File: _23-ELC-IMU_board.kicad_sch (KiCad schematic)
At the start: 4 parts

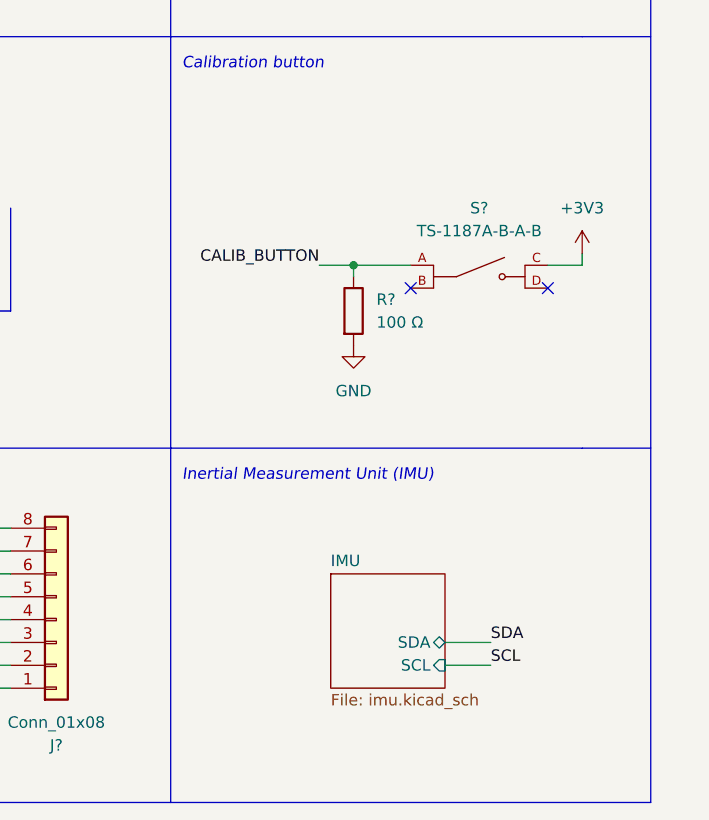
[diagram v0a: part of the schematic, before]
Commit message: Added test points for I2C
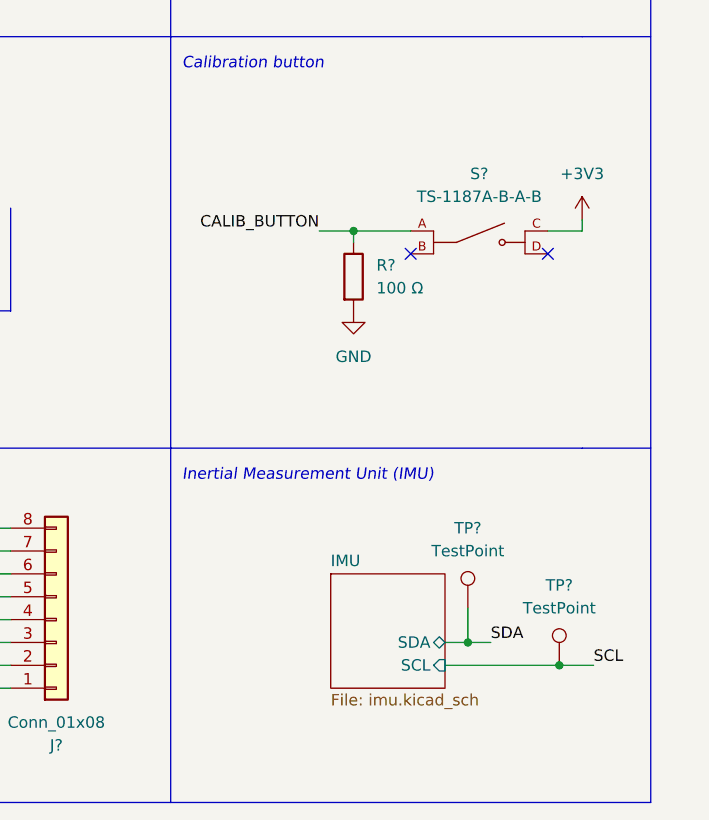
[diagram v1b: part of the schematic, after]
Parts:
- added TP? (x2): TestPoint, symbol Connector:TestPoint
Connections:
- net SCL: now also TP?.1
- net SDA: now also TP?.1
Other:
- moved on the sheet: R?, S?

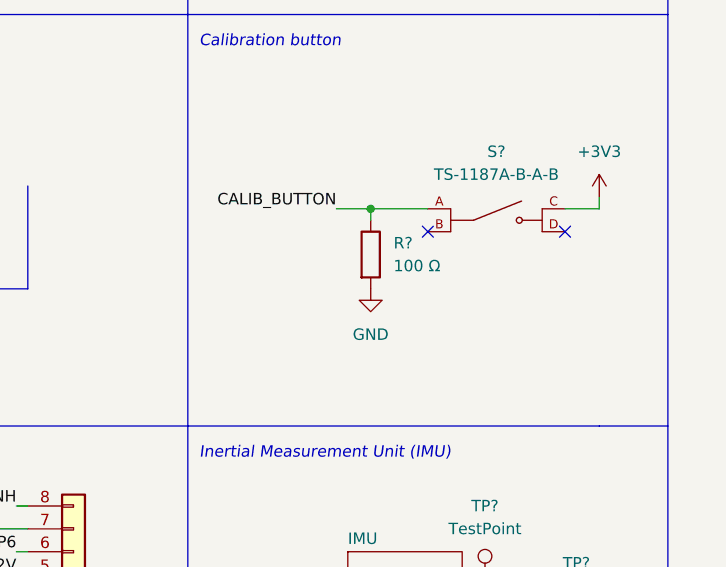
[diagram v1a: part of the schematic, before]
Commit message: 100 ohm => 1 kOhm
Pull down probably too low
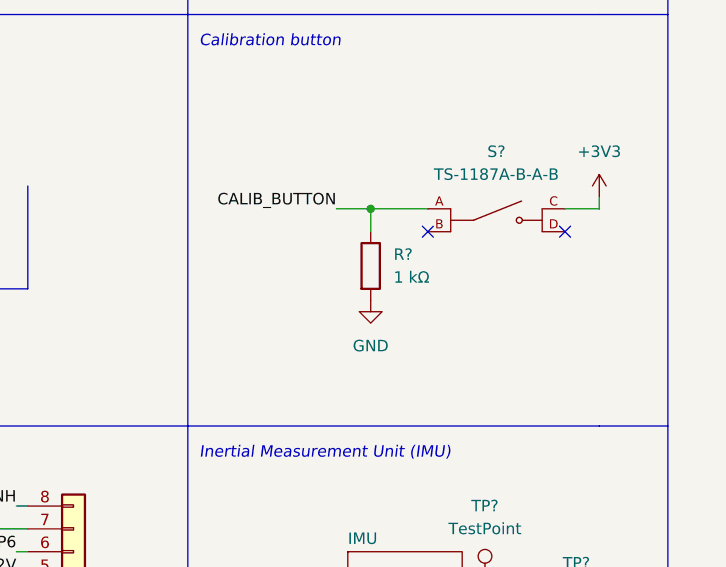
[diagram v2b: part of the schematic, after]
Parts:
- R?: value 100 Ω -> 1 kΩ
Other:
- moved on the sheet: R?
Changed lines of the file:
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@@
     (stroke (width 0) (type default) (color 0 0 0 0))
   )
-  (wire (pts (xy 180.34 95.25) (xy 180.34 96.52))
+  (wire (pts (xy 180.34 95.25) (xy 180.34 97.79))
     (stroke (width 0) (type default) (color 0 0 0 0))
   )
@@
     (pin "1")
   )
-  (symbol (lib_id "Device:R") (at 180.34 100.33 0) (unit 1)
-    (in_bom yes) (on_board yes) (fields_autoplaced)
-    (property "Reference" "R?" (id 0) (at 182.88 99.0599 0)
-      (effects (font (size 1.27 1.27)) (justify left))
-    )
-    (property "Value" "100 Ω" (id 1) (at 182.88 101.5999 0)
-      (effects (font (size 1.27 1.27)) (justify left))
-    )
-    (property "Footprint" "Resistor_SMD:R_0201_0603Metric" (id 2) (at 178.562 100.33 90)
-      (effects (font (size 1.27 1.27)) hide)
-    )
-    (property "Datasheet" "~" (id 3) (at 180.34 100.33 0)
+  (symbol (lib_id "Device:R") (at 180.34 101.6 0) (unit 1)
+    (in_bom yes) (on_board yes) (fields_autoplaced)
+    (property "Reference" "R?" (id 0) (at 182.88 100.3299 0)
+      (effects (font (size 1.27 1.27)) (justify left))
+    )
+    (property "Value" "1 kΩ" (id 1) (at 182.88 102.8699 0)
+      (effects (font (size 1.27 1.27)) (justify left))
+    )
+    (property "Footprint" "Resistor_SMD:R_0201_0603Metric" (id 2) (at 178.562 101.6 90)
+      (effects (font (size 1.27 1.27)) hide)
+    )
+    (property "Datasheet" "~" (id 3) (at 180.34 101.6 0)
       (effects (font (size 1.27 1.27)) hide)
     )
@@
     (pin "1")
   )
-  (symbol (lib_id "power:GND") (at 180.34 104.14 0) (unit 1)
-    (in_bom yes) (on_board yes) (fields_autoplaced)
-    (property "Reference" "#PWR?" (id 0) (at 180.34 110.49 0)
-      (effects (font (size 1.27 1.27)) hide)
-    )
-    (property "Value" "GND" (id 1) (at 180.34 109.22 0))
-    (property "Footprint" "" (id 2) (at 180.34 104.14 0)
-      (effects (font (size 1.27 1.27)) hide)
-    )
-    (property "Datasheet" "" (id 3) (at 180.34 104.14 0)
+  (symbol (lib_id "power:GND") (at 180.34 105.41 0) (unit 1)
+    (in_bom yes) (on_board yes) (fields_autoplaced)
+    (property "Reference" "#PWR?" (id 0) (at 180.34 111.76 0)
+      (effects (font (size 1.27 1.27)) hide)
+    )
+    (property "Value" "GND" (id 1) (at 180.34 110.49 0))
+    (property "Footprint" "" (id 2) (at 180.34 105.41 0)
+      (effects (font (size 1.27 1.27)) hide)
+    )
+    (property "Datasheet" "" (id 3) (at 180.34 105.41 0)
       (effects (font (size 1.27 1.27)) hide)
     )
@@
     )
     (path "/a06d3903-222c-4eb8-bb14-5ed150152b48"
-      (reference "R?") (unit 1) (value "100 Ω") (footprint "Resistor_SMD:R_0201_0603Metric")
+      (reference "R?") (unit 1) (value "1 kΩ") (footprint "Resistor_SMD:R_0201_0603Metric")
     )
     (path "/20fcfeb0-ed28-45b7-bc17-0a1a87e552cb/d2fa6f23-28b3-495b-8856-8c8bf7f687e9"

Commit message: Updated subsheets
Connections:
- net DIRTY_12V renamed +24V
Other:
- removed sheet Standardized VRMS
- added sheet VRMS (vrmsv2.kicad_sch)
- moved on the sheet: TP?

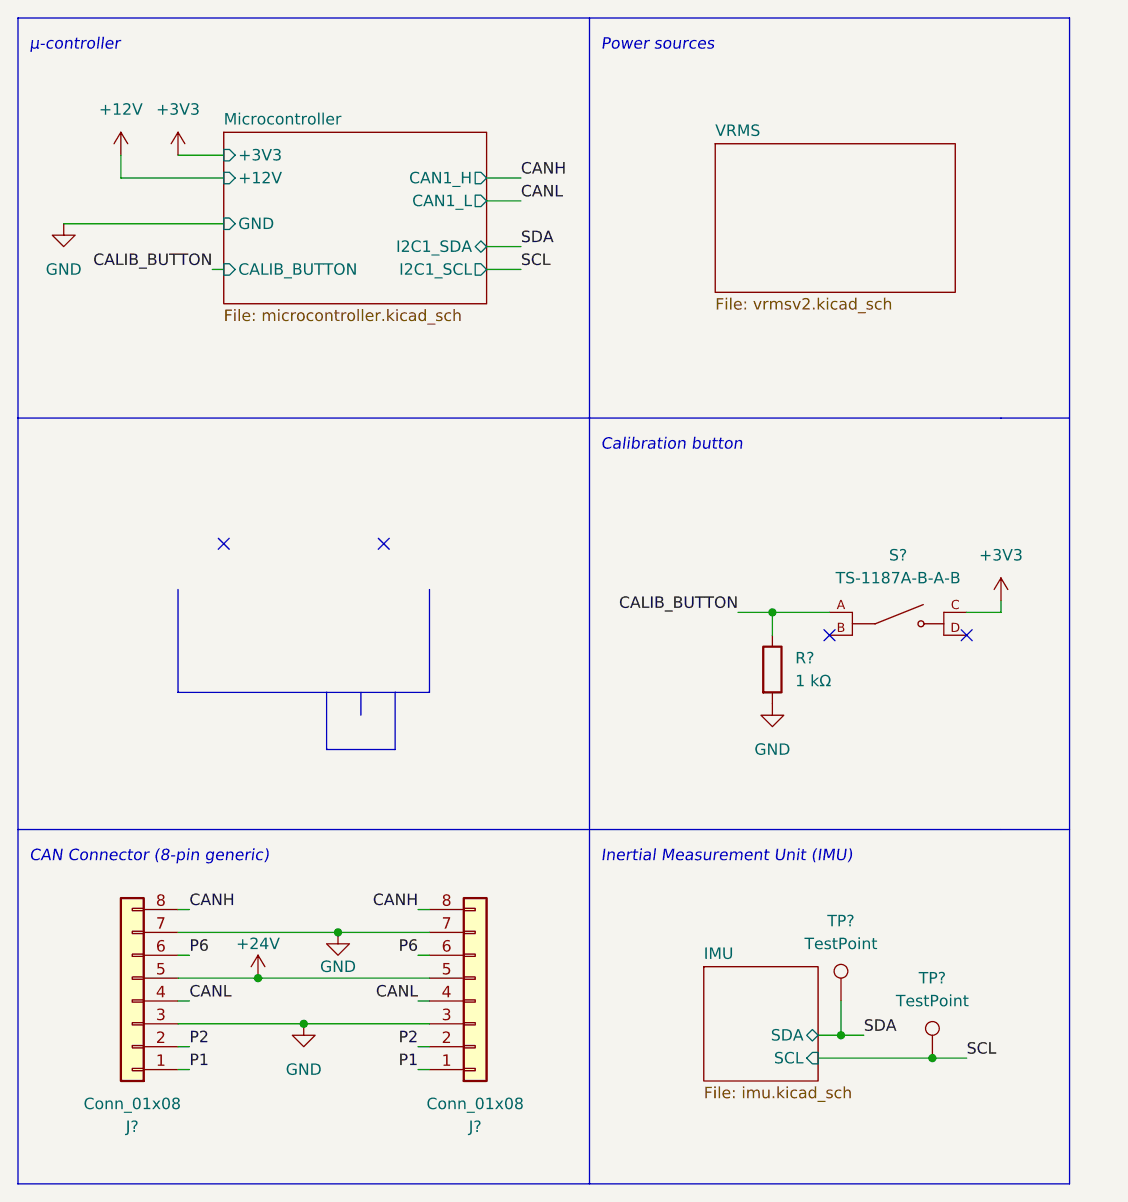
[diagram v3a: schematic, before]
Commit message: Adjusted CAN bus voltage to 5V
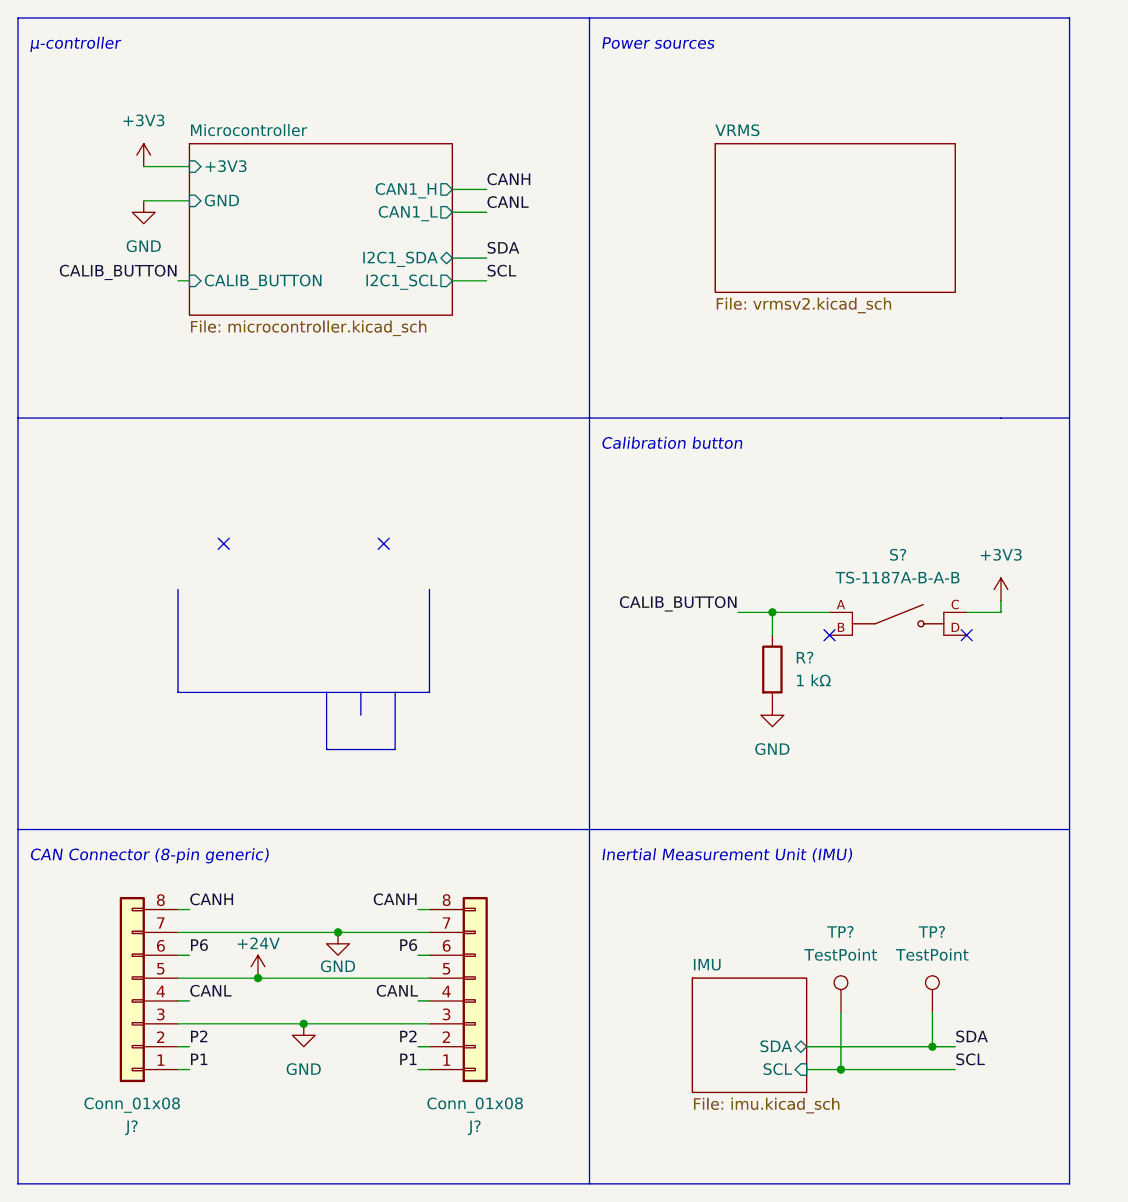
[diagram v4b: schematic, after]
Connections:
- net SCL: now also TP?.1; no longer TP?.1
- net SDA: now also TP?.1; no longer TP?.1
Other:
- sheet Microcontroller ports: added none; removed +12V
- moved on the sheet: TP?

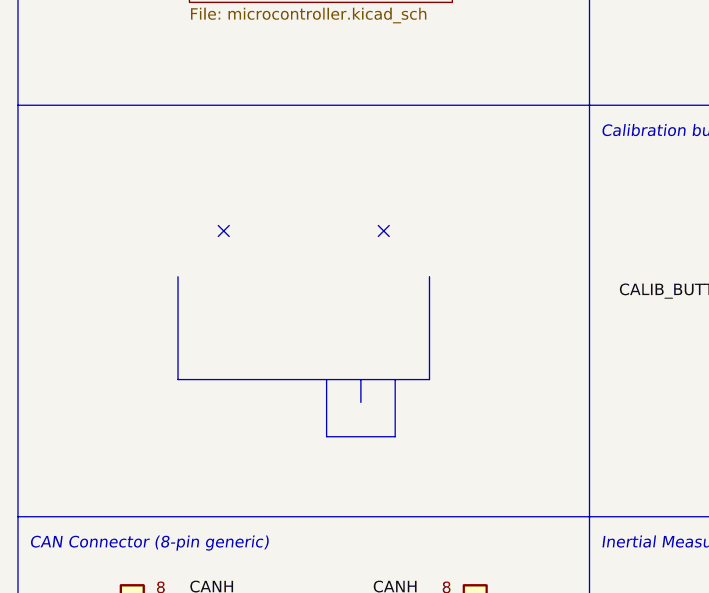
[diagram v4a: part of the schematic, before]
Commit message: Added three mounting holes
I have no idea what to do here
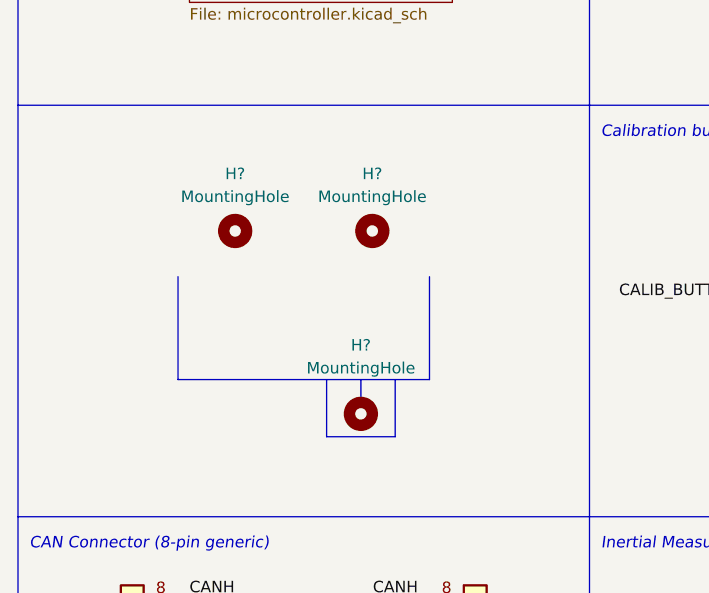
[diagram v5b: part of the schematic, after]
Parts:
- added H? (x3): MountingHole, symbol Mechanical:MountingHole
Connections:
- no-connect marks 4 -> 2
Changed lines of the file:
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@@
   (junction (at 198.12 143.51) (diameter 0) (color 0 0 0 0)
   )
-  (no_connect (at 119.38 87.63))
-  (no_connect (at 137.16 87.63))
   (no_connect (at 201.93 97.79))
   (no_connect (at 186.69 97.79))
@@
     (pin "1")
   )
+  (symbol (lib_id "Mechanical:MountingHole") (at 120.65 87.63 0) (unit 1)
+    (in_bom yes) (on_board yes)
+    (property "Reference" "H?" (id 0) (at 120.65 81.28 0))
+    (property "Value" "MountingHole" (id 1) (at 120.65 83.82 0))
+    (property "Footprint" "" (id 2) (at 120.65 87.63 0)
+      (effects (font (size 1.27 1.27)) hide)
+    )
+    (property "Datasheet" "~" (id 3) (at 120.65 87.63 0)
+      (effects (font (size 1.27 1.27)) hide)
+    )
+  )
+  (symbol (lib_id "Mechanical:MountingHole") (at 135.89 87.63 0) (unit 1)
+    (in_bom yes) (on_board yes)
+    (property "Reference" "H?" (id 0) (at 135.89 81.28 0))
+    (property "Value" "MountingHole" (id 1) (at 135.89 83.82 0))
+    (property "Footprint" "" (id 2) (at 135.89 87.63 0)
+      (effects (font (size 1.27 1.27)) hide)
+    )
+    (property "Datasheet" "~" (id 3) (at 135.89 87.63 0)
+      (effects (font (size 1.27 1.27)) hide)
+    )
+  )
   (symbol (lib_id "power:+3V3") (at 110.49 45.72 0) (unit 1)
     (in_bom yes) (on_board yes) (fields_autoplaced)
@@
     )
     (pin "1")
+  )
+  (symbol (lib_id "Mechanical:MountingHole") (at 134.62 107.95 0) (unit 1)
+    (in_bom yes) (on_board yes)
+    (property "Reference" "H?" (id 0) (at 134.62 100.33 0))
+    (property "Value" "MountingHole" (id 1) (at 134.62 102.87 0))
+    (property "Footprint" "" (id 2) (at 134.62 107.95 0)
+      (effects (font (size 1.27 1.27)) hide)
+    )
+    (property "Datasheet" "~" (id 3) (at 134.62 107.95 0)
+      (effects (font (size 1.27 1.27)) hide)
+    )
   )
   (symbol (lib_id "Device:R") (at 180.34 101.6 0) (unit 1)
@@
       (reference "F1") (unit 1) (value "2A") (footprint "Fuse:Fuse_1206_3216Metric_Pad1.42x1.75mm_HandSolder")
     )
+    (path "/356ff616-b1b1-4416-9ded-9a91fb3271e6"
+      (reference "H?") (unit 1) (value "MountingHole") (footprint "")
+    )
+    (path "/5a81ba6d-1cb8-4f90-ad37-c37491f7df47"
+      (reference "H?") (unit 1) (value "MountingHole") (footprint "")
+    )
+    (path "/8b54c01c-32c6-4484-b962-a405cc47c265"
+      (reference "H?") (unit 1) (value "MountingHole") (footprint "")
+    )
     (path "/54e69940-e60b-406d-b33c-8246d242800f/27fec5df-f50a-420e-8f18-082a387b0bca"

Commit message: Pushing assorted changes
I think I just changed a couple names
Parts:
- TP?: value TestPoint -> SDA_Test
- TP?: value TestPoint -> SCL_Test
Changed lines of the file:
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@@
     (in_bom yes) (on_board yes)
     (property "Reference" "TP?" (id 0) (at 198.12 130.81 0))
-    (property "Value" "TestPoint" (id 1) (at 198.12 133.35 0))
+    (property "Value" "SDA_Test" (id 1) (at 198.12 133.35 0))
     (property "Footprint" "" (id 2) (at 203.2 139.7 0)
       (effects (font (size 1.27 1.27)) hide)
@@
     (in_bom yes) (on_board yes)
     (property "Reference" "TP?" (id 0) (at 187.96 130.81 0))
-    (property "Value" "TestPoint" (id 1) (at 187.96 133.35 0))
+    (property "Value" "SCL_Test" (id 1) (at 187.96 133.35 0))
     (property "Footprint" "" (id 2) (at 193.04 139.7 0)
       (effects (font (size 1.27 1.27)) hide)
@@
     )
     (path "/2e20534c-db23-4779-b935-bdcdad748d27"
-      (reference "TP?") (unit 1) (value "TestPoint") (footprint "")
+      (reference "TP?") (unit 1) (value "SDA_Test") (footprint "")
     )
     (path "/f5a8a556-7cb0-4bdc-b114-48db54953dd2"
-      (reference "TP?") (unit 1) (value "TestPoint") (footprint "")
+      (reference "TP?") (unit 1) (value "SCL_Test") (footprint "")
     )
     (path "/54e69940-e60b-406d-b33c-8246d242800f/00000000-0000-0000-0000-0000634311a7"

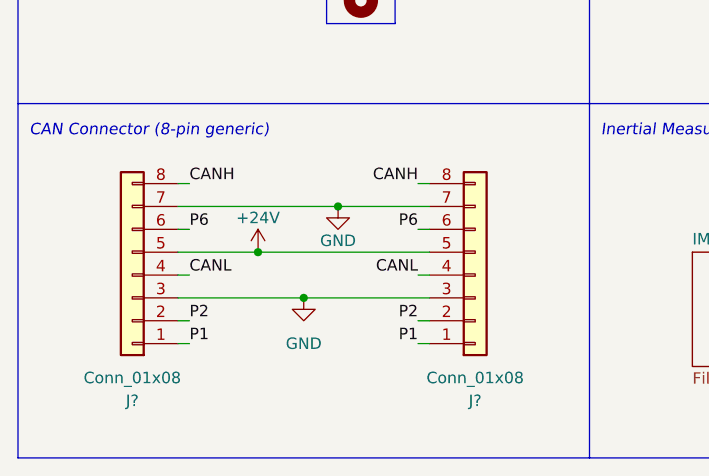
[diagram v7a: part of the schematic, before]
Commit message: Changed connector to 1x6
Will be using Deutsch DT-6
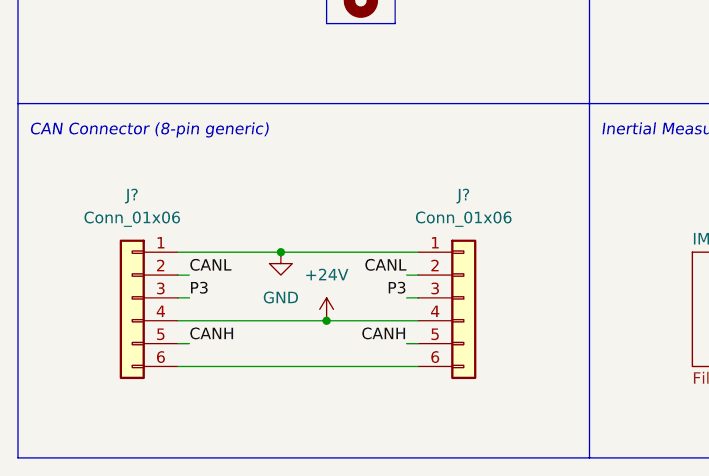
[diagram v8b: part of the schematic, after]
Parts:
- removed J? (x2): Conn_01x08, Global Libraries:348300801, symbol Connector_Generic:Conn_01x08
- added J? (x2): Conn_01x06, symbol Connector_Generic:Conn_01x06
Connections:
- net +24V: now also J?.4 (Pin_4), J?.4 (Pin_4)
- net CANH: now also J?.5 (Pin_5), J?.5 (Pin_5)
- net CANL: now also J?.2 (Pin_2), J?.2 (Pin_2)
- net GND: now also J?.1 (Pin_1), J?.1 (Pin_1)
- new net: J?.6 (Pin_6), J?.6 (Pin_6)
- new net P3: J?.3 (Pin_3), J?.3 (Pin_3)
